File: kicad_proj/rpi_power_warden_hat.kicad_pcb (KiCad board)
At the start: 4 copper layers, 65 x 56.5 mm, 68 parts, among them J1 54-00164, J2 54-00164, J3 54-00003, J4 Raspberry Pi SMT connector, Q1 DMG2305UX-7, Q2 DMG2305UX-7, U1 INA260, U10 SN74AHC1G08DBVR, U2 INA260, U3 CAT24C32WI-GT3, U4 TPS563200, U5 DMMT5401-7-F, U6 TPS563200, U7 DMMT5401-7-F, U8 TPS22810DBVR, U9 SN74AHC1G08DBVR

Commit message: modify general soldermask expansion to 0 and generate outputs.
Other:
- rule pad_to_mask_clearance: 0.038 -> 0

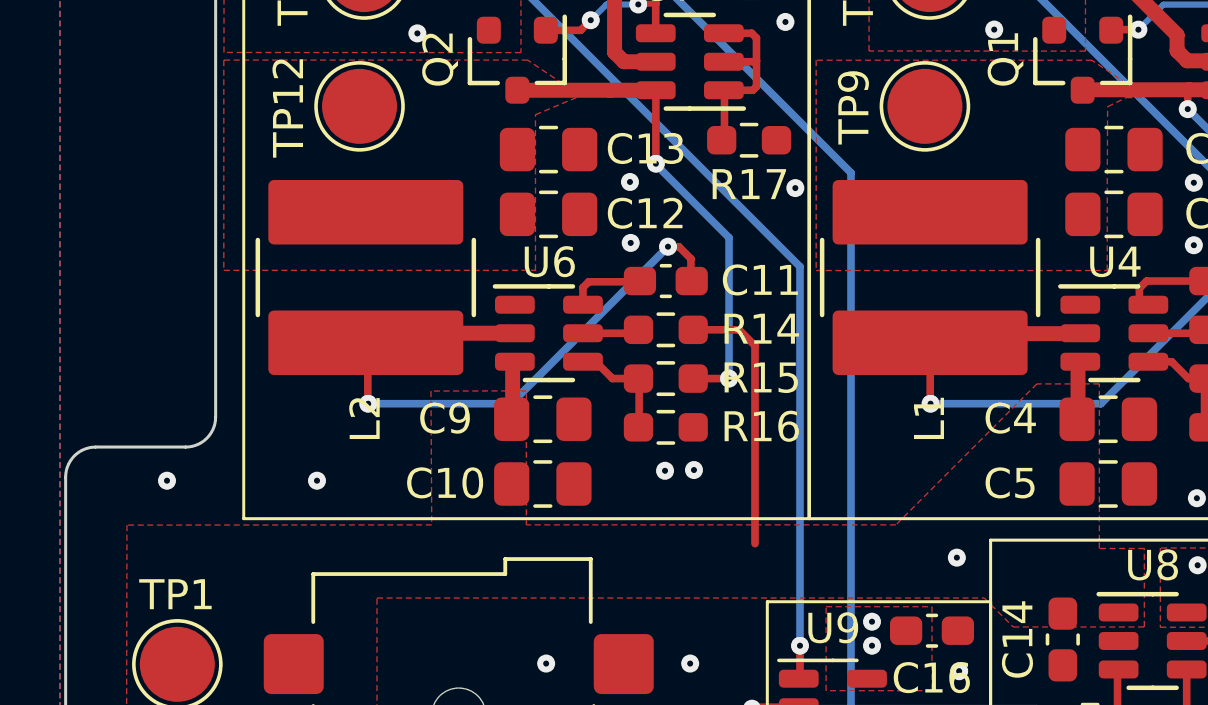
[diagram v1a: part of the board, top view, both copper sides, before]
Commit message: fix: replace some components out of stock in lcsc
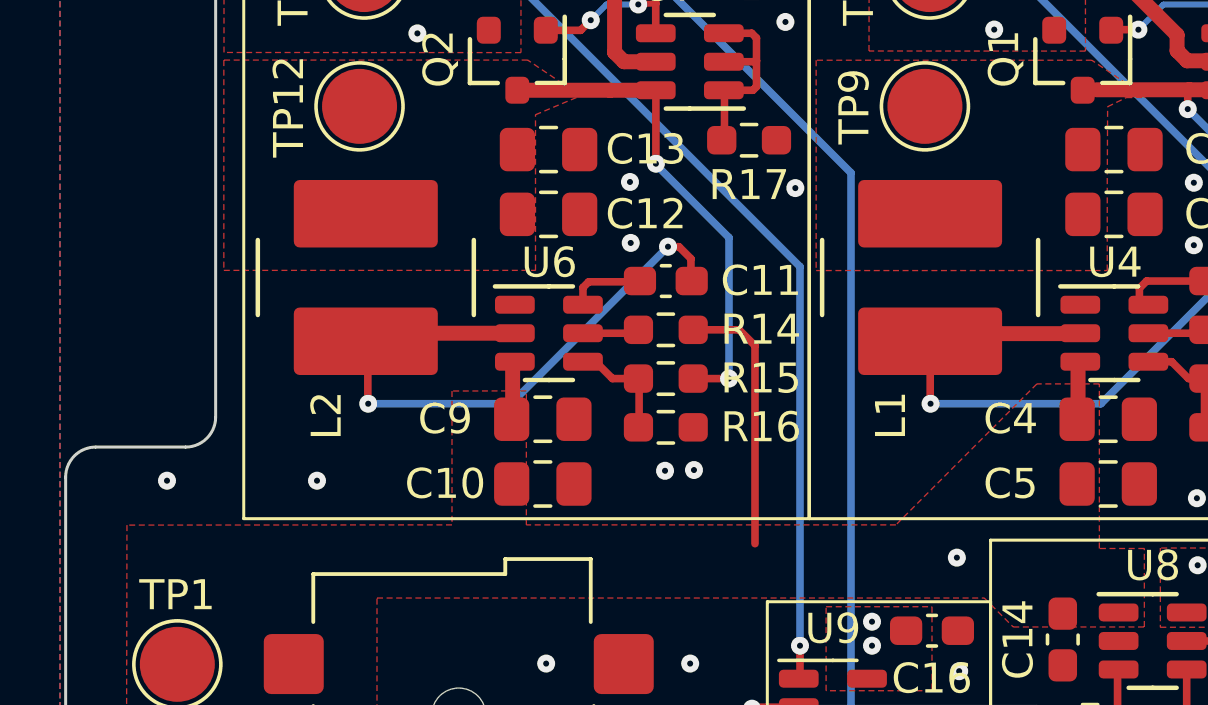
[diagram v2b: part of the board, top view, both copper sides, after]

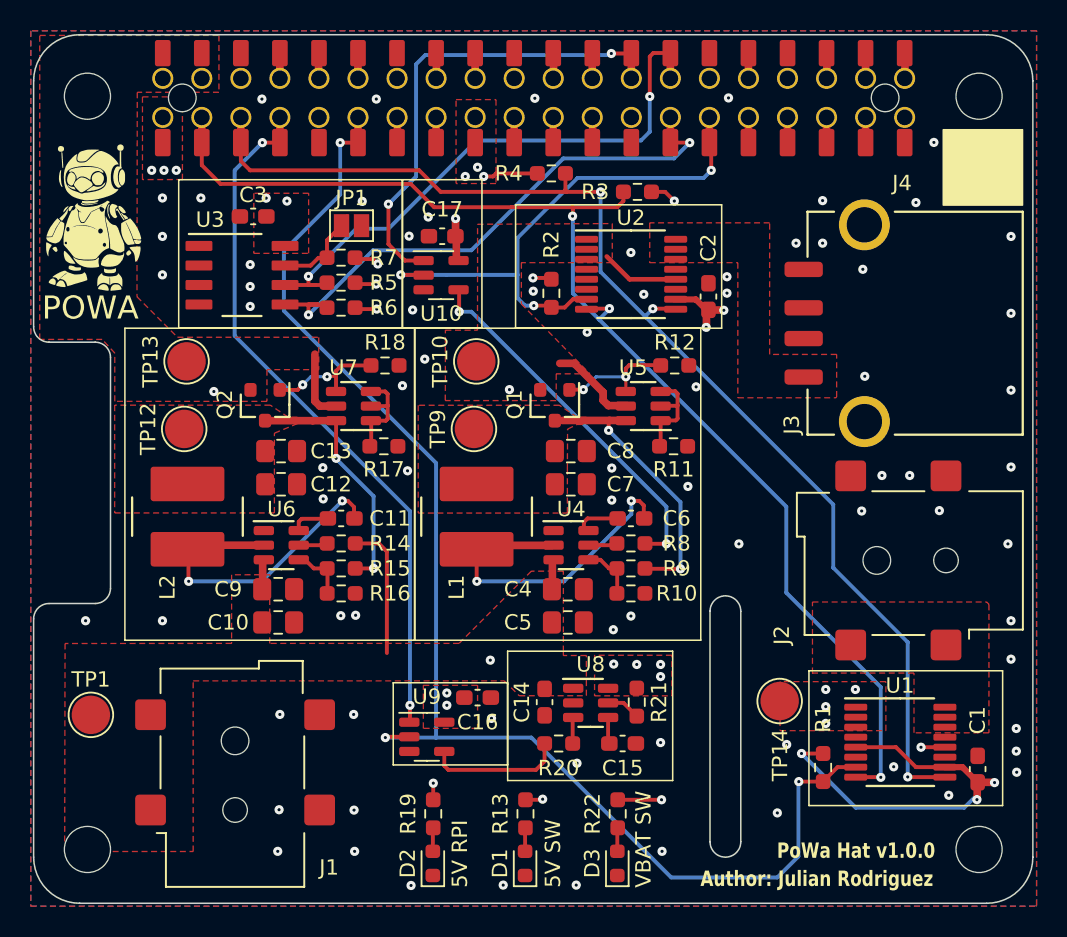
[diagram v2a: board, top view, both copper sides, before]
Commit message: replaced almost all the components out of stock (only tensility connectors: USB and jack needs to be replaced)
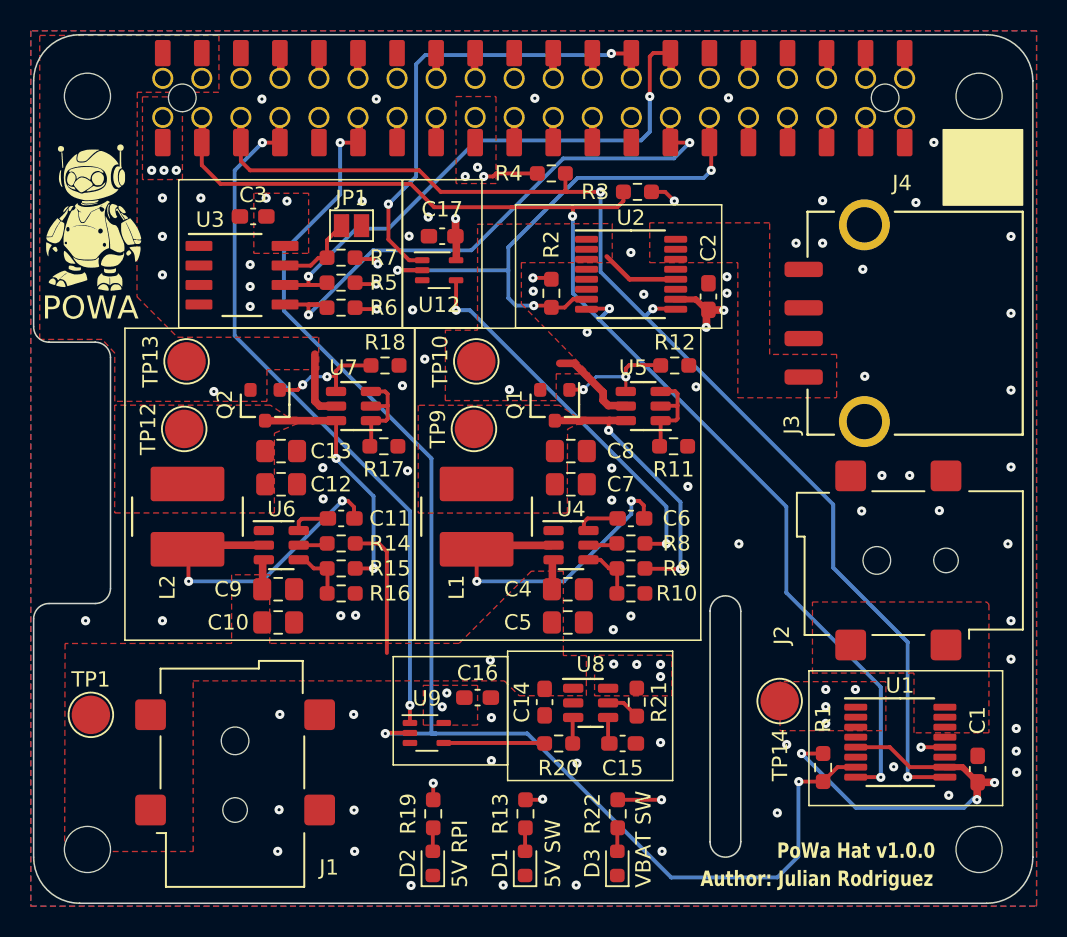
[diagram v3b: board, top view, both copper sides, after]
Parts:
- removed U10: SN74AHC1G08DBVR, rpi_power_warden_hat:SOT-23-5
- added U12: SN74AHC1G08DCK, rpi_power_warden_hat:SOT-353, F.Cu at (153.3, 85.1)
- U9: value SN74AHC1G08DBVR -> SN74AHC1G08DCK; footprint rpi_power_warden_hat:SOT-23-5 -> rpi_power_warden_hat:SOT-353
- moved U9 0.25 mm to (152.5, 115.2)
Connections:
- net /rpi/CE0_SPI0/GPIO08 renamed /rpi/CE0_SPI0/GPIO08_1
- net /rpi/GPIO14/UART_TXD_1 renamed /rpi/GPIO14/UART_TXD
- net /rpi/GPIO15/UART_RXD_1 renamed /rpi/GPIO15/UART_RXD
- net /rpi/GPIO16/SP1_CE2_1 renamed /rpi/GPIO16/SP1_CE2
- net /rpi/GPIO19/SPI1_MISO_1 renamed /rpi/GPIO19/SPI1_MISO
- net /rpi/GPIO21/SPI1_CLK renamed /rpi/GPIO21/SPI1_CLK_1
- net /rpi/GPIO22/SDIO_CLK_1 renamed /rpi/GPIO22/SDIO_CLK
- net /rpi/GPIO23/SDIO_CMD renamed /rpi/GPIO23/SDIO_CMD_1
- net /rpi/GPIO24/SDIO_DAT0 renamed /rpi/GPIO24/SDIO_DAT0_1
- net /rpi/GPIO25/SDIO_DAT1_1 renamed /rpi/GPIO25/SDIO_DAT1
- net /rpi/GPIO26/SDIO_DAT2_1 renamed /rpi/GPIO26/SDIO_DAT2
- net /rpi/GPIO27/SDIO_DAT3 renamed /rpi/GPIO27/SDIO_DAT3_1
- net /rpi/MISO_SPI0/GPIO09_1 renamed /rpi/MISO_SPI0/GPIO09
- net /rpi/MOSI_SPI0/GPIO10_1 renamed /rpi/MOSI_SPI0/GPIO10
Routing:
- net /and_vbat/Y: track 8.96 -> 6.57 mm
- net /and_5v/Y: track 24.3 -> 24.9 mm
- net GND: vias 76 -> 77

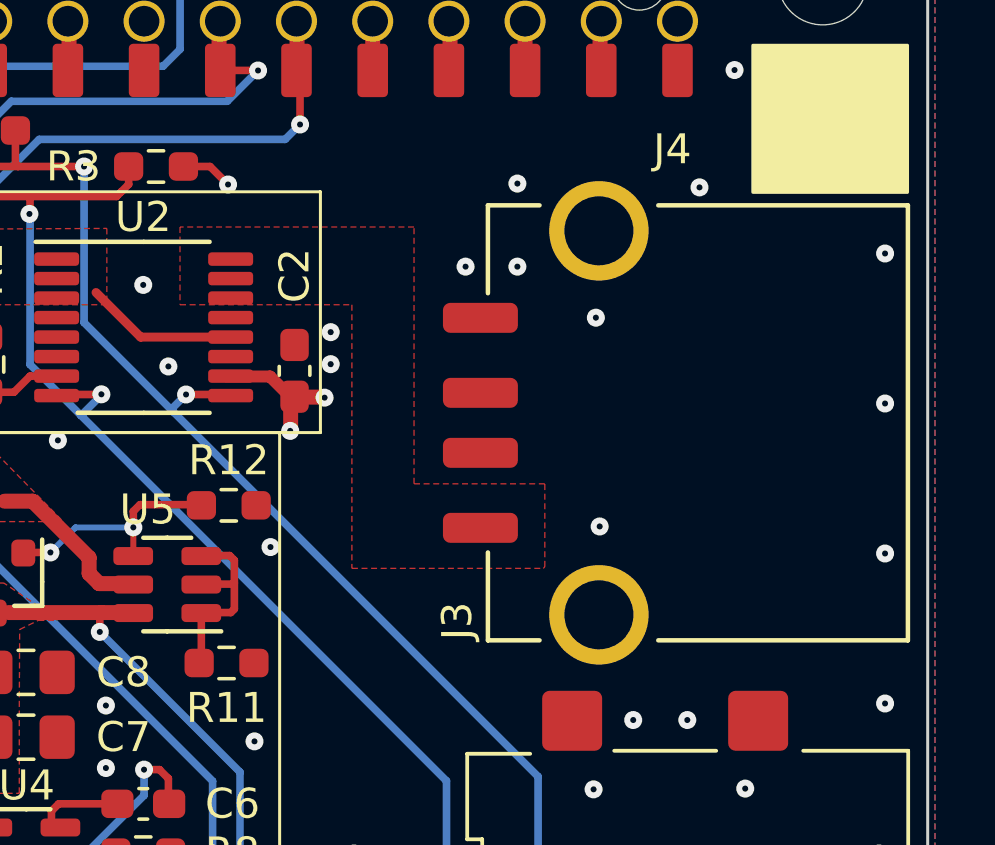
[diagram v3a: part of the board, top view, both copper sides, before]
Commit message: changed usb A for an usb C with more stock
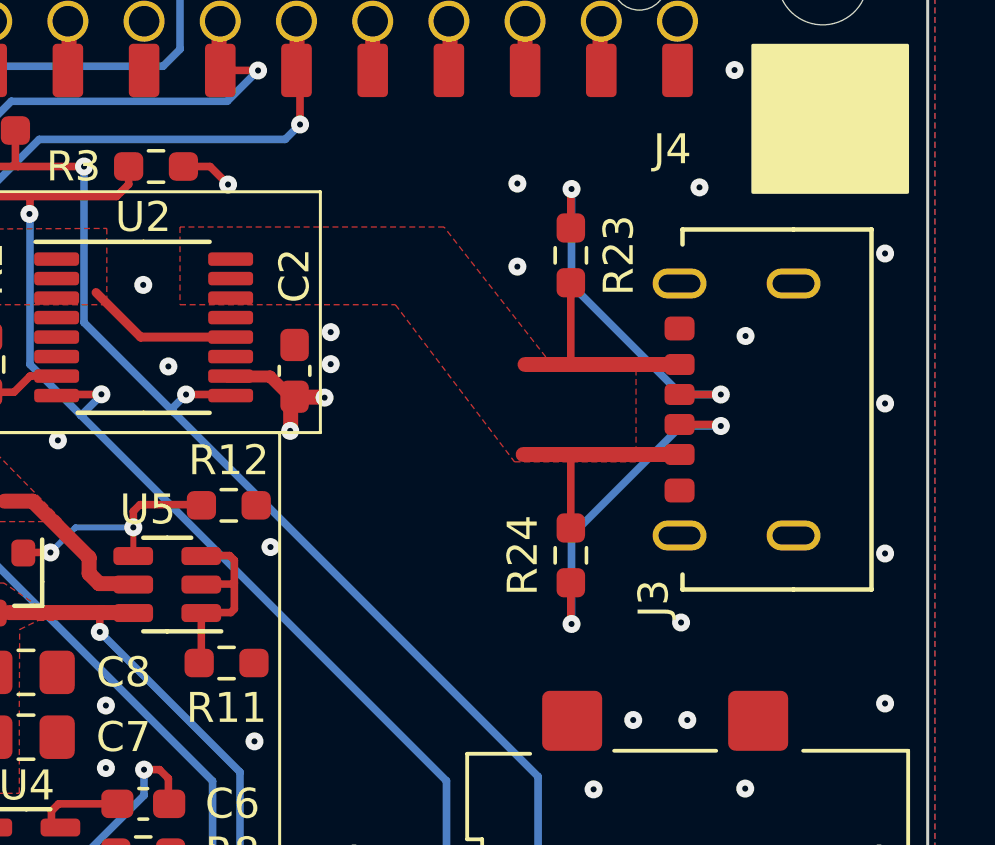
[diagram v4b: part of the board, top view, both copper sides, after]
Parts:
- added R23: 5.1 kΩ, Resistor_SMD:R_0603_1608Metric_Pad0.98x0.95mm_HandSolder, F.Cu at (180.0, 83.0)
- added R24: 5.1 kΩ, Resistor_SMD:R_0603_1608Metric_Pad0.98x0.95mm_HandSolder, F.Cu at (180.0, 93.0)
- J3: value 54-00003 -> TYPE-C 6P; footprint rpi_power_warden_hat:TENSILITY_54-00003 -> rpi_power_warden_hat:SHOU_HAN_TYPE-C-6P
- moved J3 6.50 mm to (187.4, 88.1)
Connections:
- net /rpi/CE0_SPI0/GPIO08_1 renamed /rpi/CE0_SPI0/GPIO08
- net /rpi/GPIO12/PWM0_1 renamed /rpi/GPIO12/PWM0
- net /rpi/GPIO13/PWM1 renamed /rpi/GPIO13/PWM1_1
- net /rpi/GPIO15/UART_RXD renamed /rpi/GPIO15/UART_RXD_1
- net /rpi/GPIO16/SP1_CE2 renamed /rpi/GPIO16/SP1_CE2_1
- net /rpi/GPIO18/SPI1_CE0 renamed /rpi/GPIO18/SPI1_CE0_1
- net /rpi/GPIO21/SPI1_CLK_1 renamed /rpi/GPIO21/SPI1_CLK
- net /rpi/GPIO22/SDIO_CLK renamed /rpi/GPIO22/SDIO_CLK_1
- net /rpi/GPIO24/SDIO_DAT0_1 renamed /rpi/GPIO24/SDIO_DAT0
- net /rpi/SCLK_SPI0/GPIO11_1 renamed /rpi/SCLK_SPI0/GPIO11
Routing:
- net /current_sensor_5V/+VCC_OUT: track 0.00 -> 15.6 mm
- net Net-(J3-CC2): track 0.00 -> 12.4 mm, vias 0 -> 2
- net Net-(J3-CC1): track 0.00 -> 12.2 mm, vias 0 -> 2
- net /rpi/SCLK_SPI0/GPIO11_1: track 0.00 -> 1.64 mm
- net /rpi/SCLK_SPI0/GPIO11: track 1.64 -> 0.00 mm
- net /rpi/GPIO24/SDIO_DAT0_1: track 0.00 -> 1.64 mm
- net /rpi/GPIO24/SDIO_DAT0: track 1.64 -> 0.00 mm
- net /rpi/GPIO22/SDIO_CLK_1: track 1.64 -> 0.00 mm
- net /rpi/GPIO22/SDIO_CLK: track 0.00 -> 1.64 mm
- net /rpi/GPIO21/SPI1_CLK_1: track 0.00 -> 1.64 mm
- net /rpi/GPIO21/SPI1_CLK: track 1.64 -> 0.00 mm
- net /rpi/GPIO18/SPI1_CE0_1: track 1.64 -> 0.00 mm
- net /rpi/GPIO18/SPI1_CE0: track 0.00 -> 1.64 mm
- net /rpi/GPIO15/UART_RXD_1: track 1.64 -> 0.00 mm
- net /rpi/GPIO15/UART_RXD: track 0.00 -> 1.64 mm
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
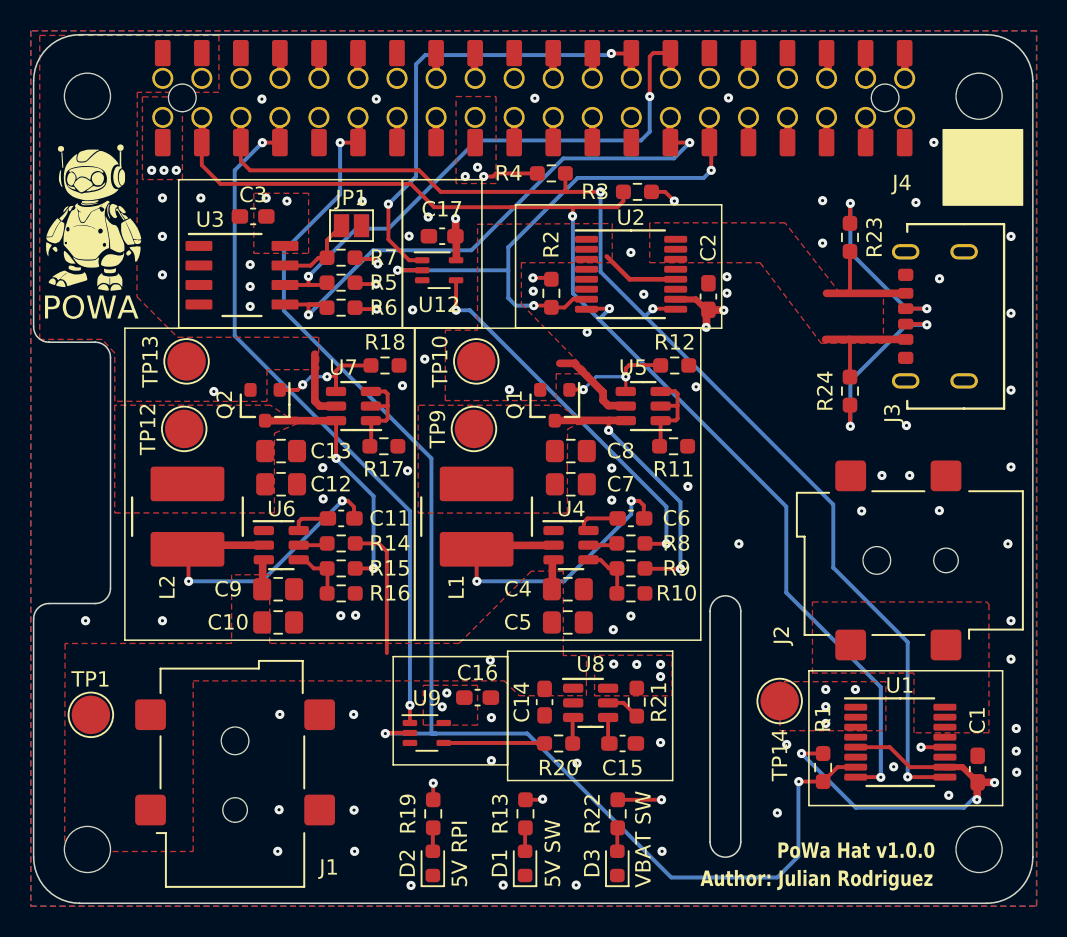
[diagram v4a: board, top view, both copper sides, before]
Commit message: replace DC jack for one with stock
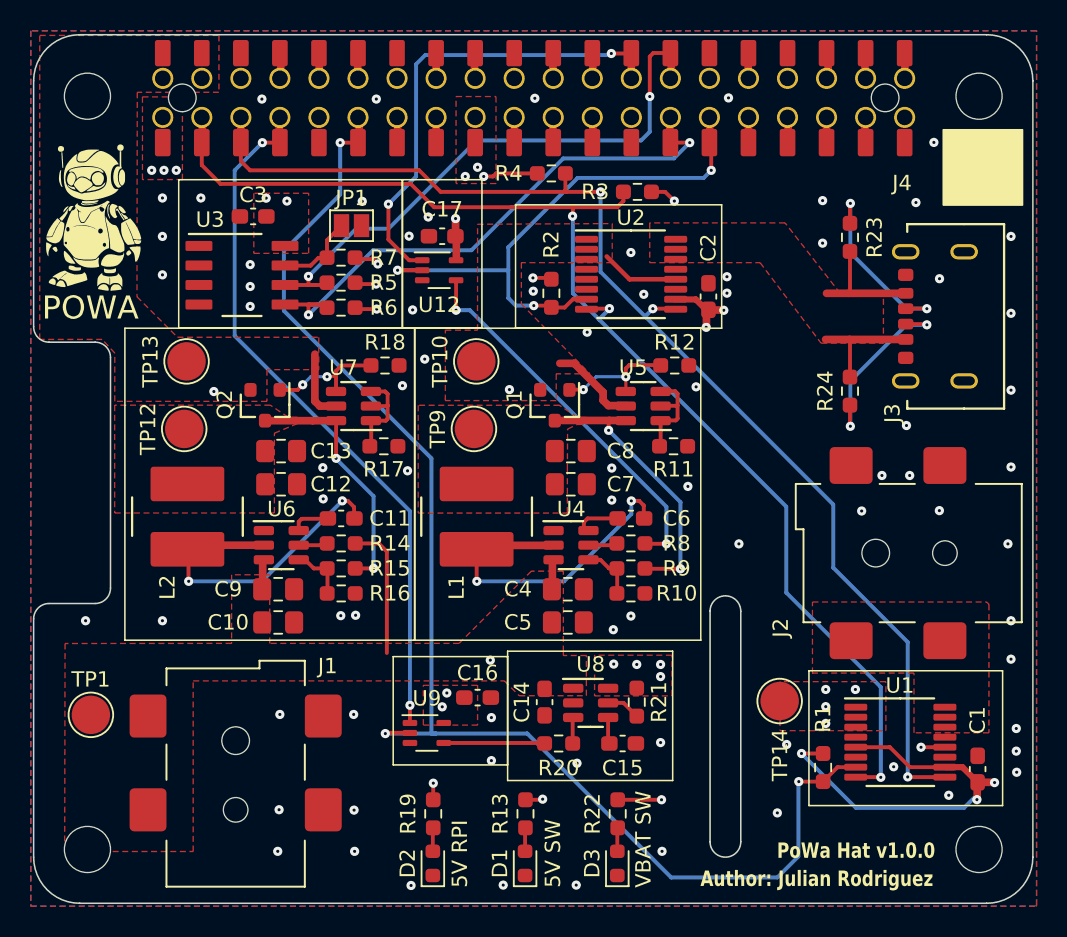
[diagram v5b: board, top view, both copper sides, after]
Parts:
- J1, J2: value 54-00164 -> DC-005-5A-2.5-SMT; footprint rpi_power_warden_hat:TENSILITY_54-00164 -> rpi_power_warden_hat:XKB_DC-005-5A-2.5-SMT
- moved J2 0.48 mm to (183.9, 103.5)
